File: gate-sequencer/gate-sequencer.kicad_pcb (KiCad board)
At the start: 2 copper layers, 168.4 x 345.6 mm, 172 parts, among them J1 Power, J10 Gate 6, J11 Gate 7, J12 Gate 8, J13 Gate 9, J14 Gate 10, J15 Gate 11, J16 Gate 13, J17 Gate 12, J18 Gate 14, J19 Gate 15, J2 Power, J20 Gate 16, J21 Conn_01x34_Socket, J22 Clock, J23 Gate 1, J24 LED, J25 Gate 2, J26 LED, J27 LED, J28 LED, J29 Gate 3, J3 Power, J30 Gate 4, J31 Gate 5, J32 LED, J33 LED, J34 Gate 6, J35 LED, J36 LED, J37 Gate 7, J38 Gate 8, J39 LED, J4 Clock, J40 Gate 9, J41 LED, J42 Gate 10, J43 LED, J44 Gate 11, J45 LED, J46 LED, J47 Gate 13, J48 Gate 12, J49 Gate 14, J5 Gate 1, J50 LED, J51 Gate 15, J52 LED, J53 LED, J54 Gate 16, J55 Conn_01x34_Pin, J6 Gate 2, J7 Gate 3, J8 Gate 5, J9 Gate 4, SW1 Mode 2, SW10 S3, SW11 S4, SW12 S5, SW13 S6, SW14 S7, SW15 S8, SW16 S9, SW17 S10, SW18 S11, SW19 S12, SW2 Mode, SW20 S13, SW21 S14, SW22 S15, SW23 S16, SW3 Clock Source, SW4 X1, SW5 X2, SW6 X3, SW7 X4, SW8 S1, SW9 S2

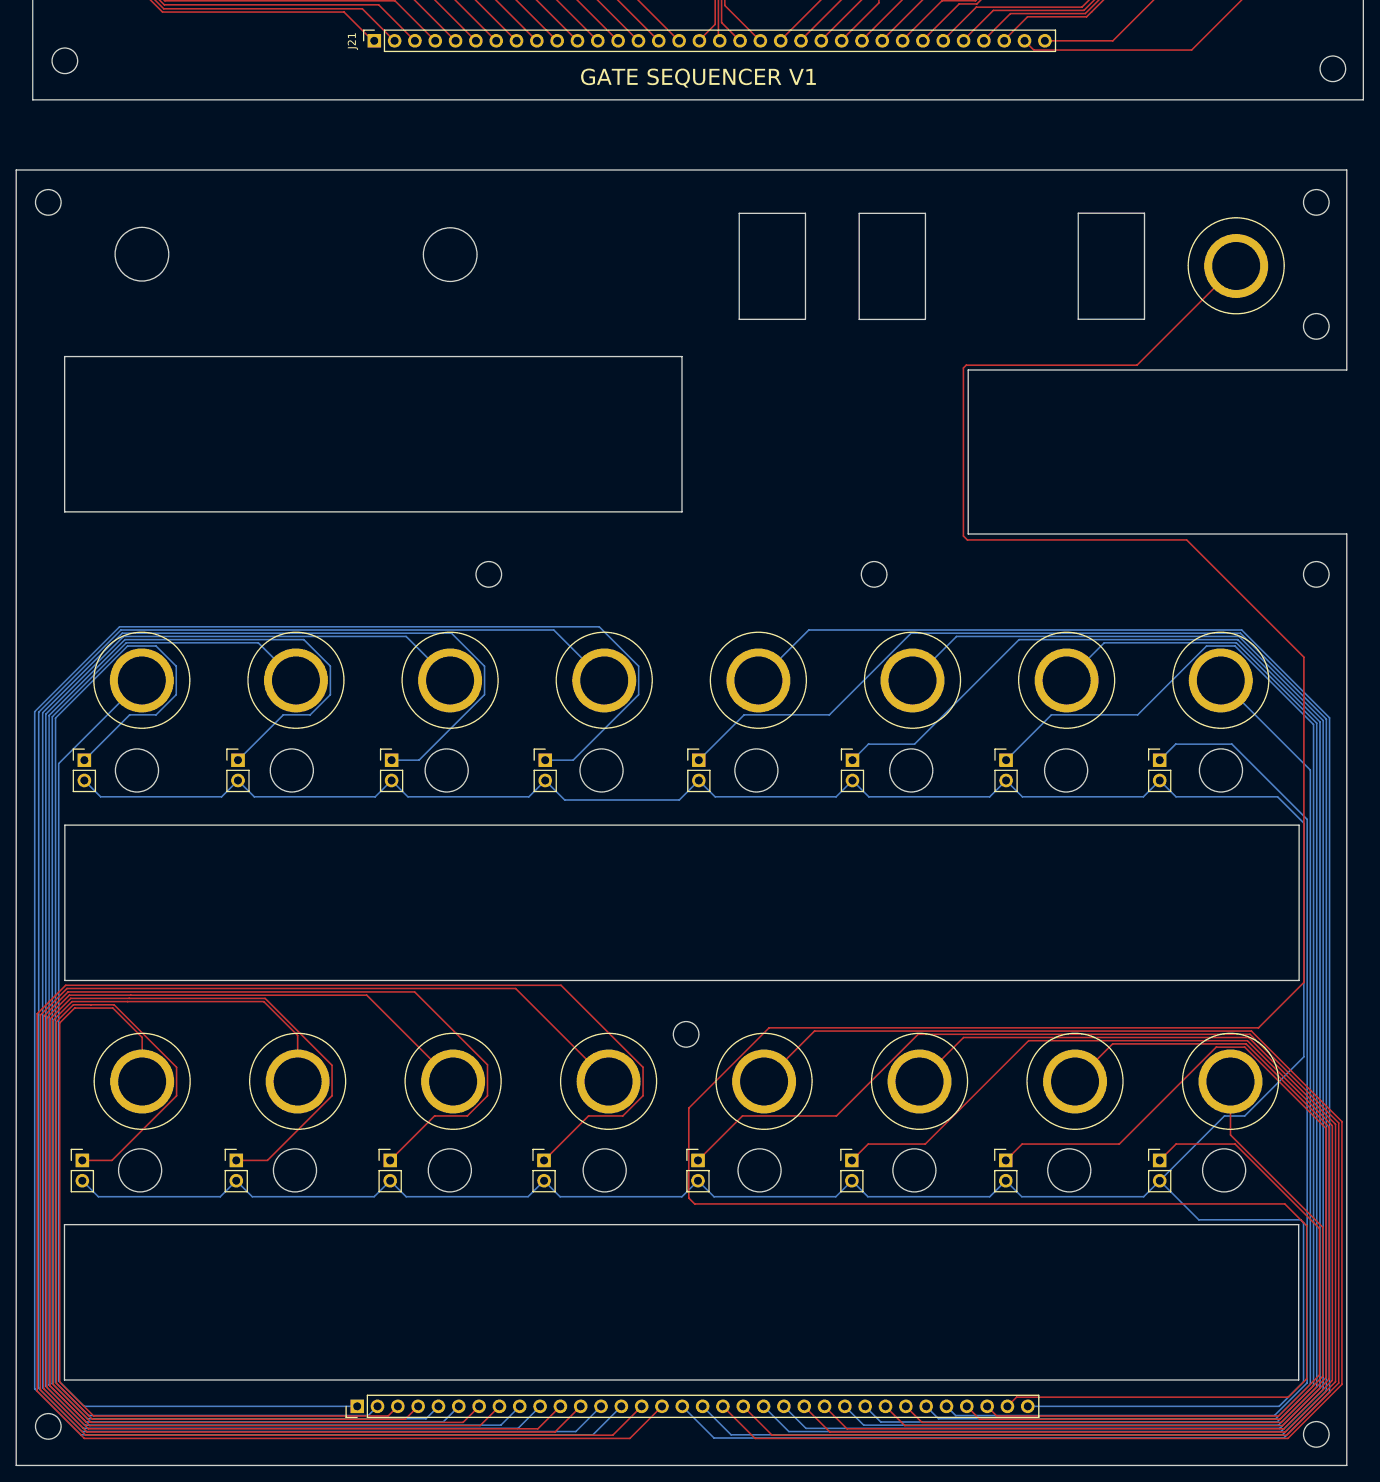
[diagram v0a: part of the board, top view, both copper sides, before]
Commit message: Start firmware for gate sequencer
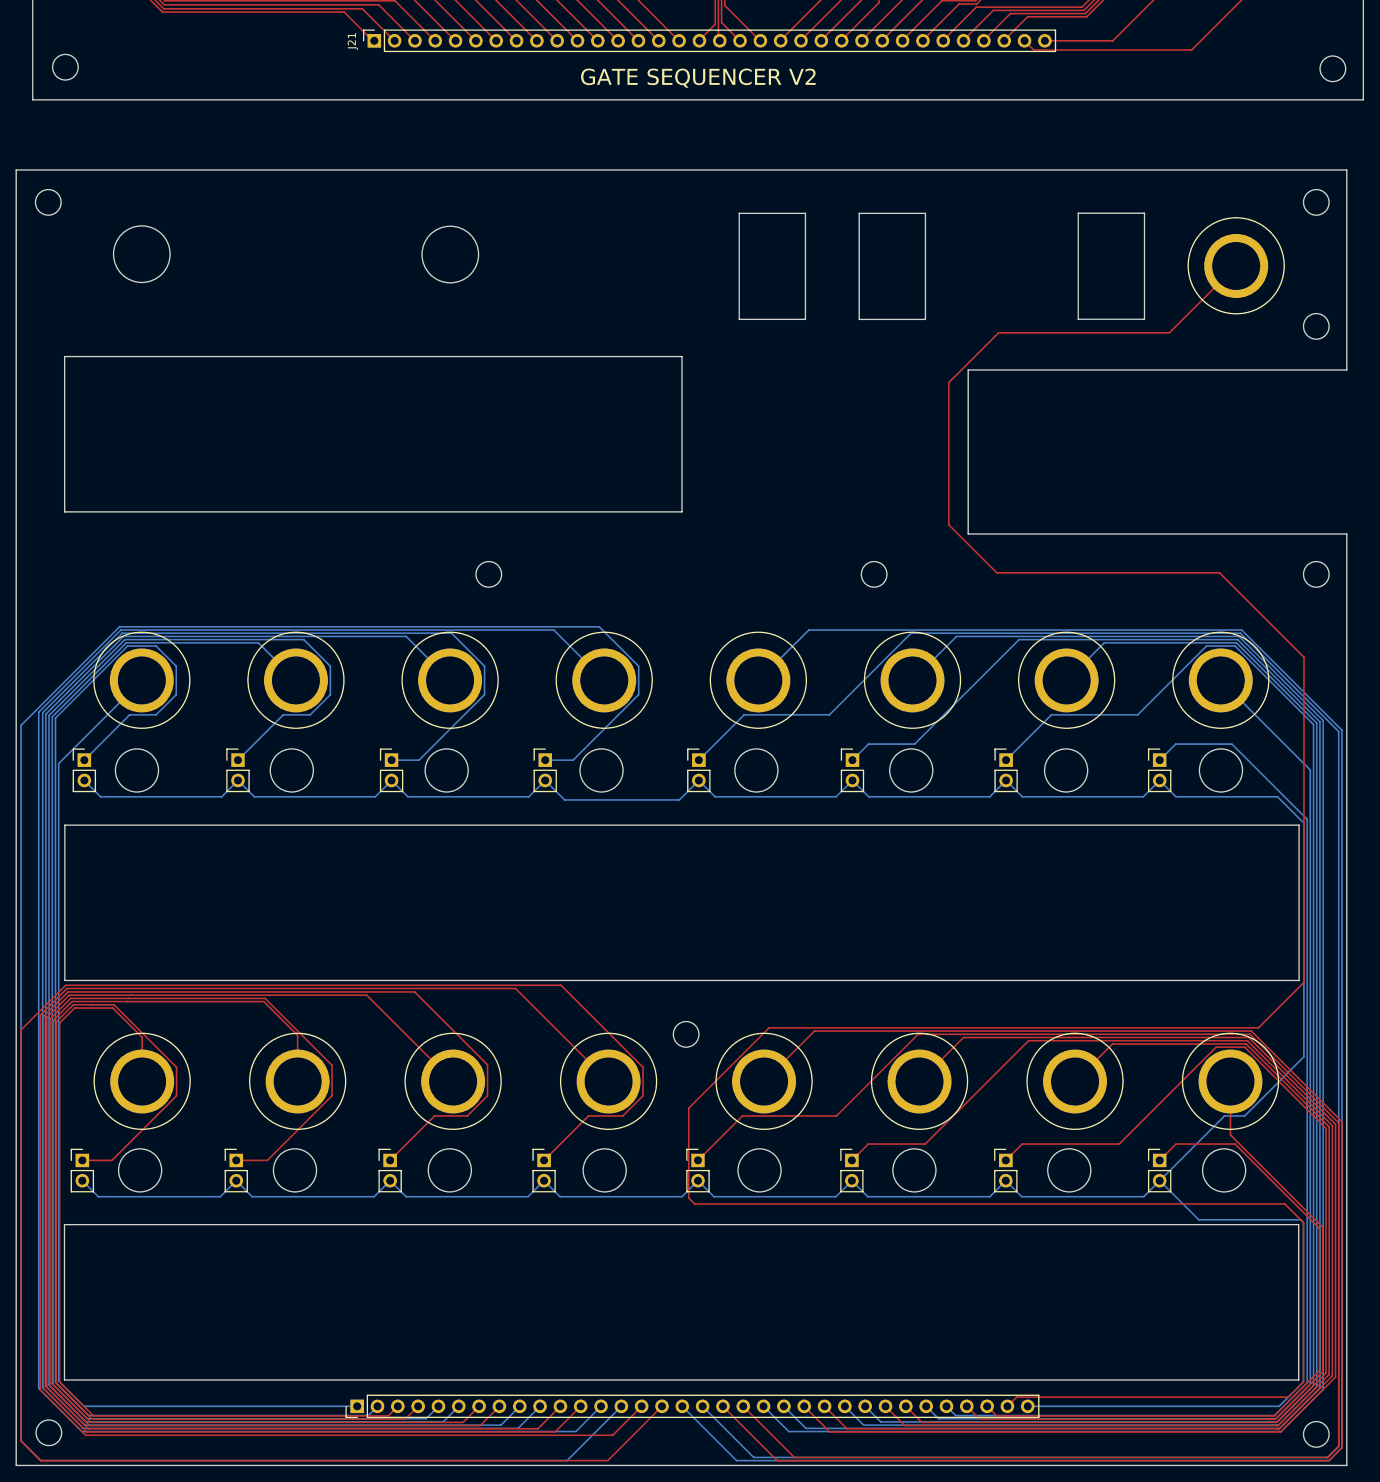
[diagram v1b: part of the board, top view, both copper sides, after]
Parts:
- moved REF** 0.81 mm to (20.5, 347.5)
- moved REF** 0.81 mm to (22.6, 176.8)
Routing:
- net Net-(J28-Pin_1): track 262.4 -> 271.3 mm
- net Net-(J45-Pin_1): track 230.1 -> 238.9 mm
- net Net-(J31-Pin_1): track 247.8 -> 256.4 mm
- net Net-(J32-Pin_1): track 255.1 -> 263.7 mm
- net Net-(J47-Pin_1): track 194.2 -> 201.2 mm
- net Net-(J46-Pin_1): track 202.4 -> 209.3 mm
- net Net-(J22-Pin_1): track 381.2 -> 382.6 mm
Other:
- outline, holes or cut-outs redrawn
- board text added: "GATE SEQUENCER V2"
- board text removed: "GATE SEQUENCER V1"

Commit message: Update some designs
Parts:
- added REF**: MountingHole_3.2mm_M3, MountingHole:MountingHole_3.2mm_M3, F.Cu at (44.7, 280.2)
- added REF**: MountingHole_3.2mm_M3, MountingHole:MountingHole_3.2mm_M3, F.Cu at (160.3, 280.2)
- added REF**: MountingHole_3.2mm_M3, MountingHole:MountingHole_3.2mm_M3, F.Cu at (161.4, 330.2)
- added REF**: MountingHole_3.2mm_M3, MountingHole:MountingHole_3.2mm_M3, F.Cu at (45.5, 91.6)
- added REF**: MountingHole_3.2mm_M3, MountingHole:MountingHole_3.2mm_M3, F.Cu at (161.1, 91.6)
- added REF**: MountingHole_3.2mm_M3, MountingHole:MountingHole_3.2mm_M3, F.Cu at (162.2, 141.6)
- added REF**: MountingHole_3.2mm_M3, MountingHole:MountingHole_3.2mm_M3, F.Cu at (44.9, 330.2)
- added REF**: MountingHole_3.2mm_M3, MountingHole:MountingHole_3.2mm_M3, F.Cu at (45.6, 141.6)
- moved REF** 32.7 mm to (103.1, 330.2)
- moved J23 28.2 mm to (35.1, 281.5)
- moved J24 28.2 mm to (27.9, 291.4)
- moved J25 28.2 mm to (54.4, 281.5)
- moved J26 28.2 mm to (47.1, 291.4)
- moved J27 28.2 mm to (66.3, 291.4)
- moved J28 28.2 mm to (85.5, 291.4)
- moved J29 28.2 mm to (73.6, 281.5)
- moved J30 28.2 mm to (92.9, 281.5)
- moved J31 28.2 mm to (112.2, 281.5)
- moved J32 28.2 mm to (104.7, 291.4)
- moved J33 28.2 mm to (123.9, 291.4)
- moved J34 28.2 mm to (131.4, 281.5)
- moved J35 28.2 mm to (162.3, 291.4)
- moved J36 28.2 mm to (143.1, 291.4)
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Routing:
- net Net-(D20-A): track 112.8 -> 115.6 mm
- net Net-(J12-Pin_1): track 135.8 -> 138.6 mm
- net Net-(J21-Pin_5): track 134.6 -> 137.2 mm
- net Net-(D6-A): track 115.6 -> 118.1 mm
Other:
- board size 168.4 x 345.6 mm -> 167.1 x 363.5 mm

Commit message: Gate sequencer fixes
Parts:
- added D37: 1N4148, Diode_THT:D_DO-35_SOD27_P7.62mm_Horizontal, F.Cu at (36.3, 109.3)
- added D38: 1N4148, Diode_THT:D_DO-35_SOD27_P7.62mm_Horizontal, F.Cu at (113.8, 108.9)
- added D39: 1N4148, Diode_THT:D_DO-35_SOD27_P7.62mm_Horizontal, F.Cu at (36.3, 159.2)
- added D40: 1N4148, Diode_THT:D_DO-35_SOD27_P7.62mm_Horizontal, F.Cu at (113.2, 159.4)
- added D41: 1N4148, Diode_THT:D_DO-35_SOD27_P7.62mm_Horizontal, F.Cu at (55.4, 159.3)
- added D42: 1N4148, Diode_THT:D_DO-35_SOD27_P7.62mm_Horizontal, F.Cu at (132.6, 109.5)
- added D43: 1N4148, Diode_THT:D_DO-35_SOD27_P7.62mm_Horizontal, F.Cu at (55.8, 109.5)
- added D44: 1N4148, Diode_THT:D_DO-35_SOD27_P7.62mm_Horizontal, F.Cu at (132.8, 159.5)
- added D45: 1N4148, Diode_THT:D_DO-35_SOD27_P7.62mm_Horizontal, F.Cu at (75.1, 109.5)
- added D46: 1N4148, Diode_THT:D_DO-35_SOD27_P7.62mm_Horizontal, F.Cu at (152.3, 109.5)
- added D47: 1N4148, Diode_THT:D_DO-35_SOD27_P7.62mm_Horizontal, F.Cu at (74.6, 159.5)
- added D48: 1N4148, Diode_THT:D_DO-35_SOD27_P7.62mm_Horizontal, F.Cu at (152.1, 159.5)
- added D49: 1N4148, Diode_THT:D_DO-35_SOD27_P7.62mm_Horizontal, F.Cu at (94.5, 109.6)
- added D50: 1N4148, Diode_THT:D_DO-35_SOD27_P7.62mm_Horizontal, F.Cu at (171.6, 109.5)
- added D51: 1N4148, Diode_THT:D_DO-35_SOD27_P7.62mm_Horizontal, F.Cu at (94.1, 159.5)
- added D52: 1N4148, Diode_THT:D_DO-35_SOD27_P7.62mm_Horizontal, F.Cu at (171.1, 159.5)
- moved R14 10.7 mm to (118.0, 98.9), turned to -90 degrees
- moved R26 10.6 mm to (41.0, 149.0), turned to -90 degrees
- moved R10 10.4 mm to (40.5, 99.2), turned to -90 degrees
- moved R33 10.3 mm to (176.0, 149.3), turned to -90 degrees
- moved R32 10.2 mm to (157.0, 149.5), turned to -90 degrees
- moved R16 10.2 mm to (156.5, 99.4), turned to -90 degrees
- moved R28 10.2 mm to (79.5, 149.4), turned to -90 degrees
- moved R29 10.2 mm to (99.0, 149.5), turned to -90 degrees
- moved R31 10.2 mm to (137.5, 149.5), turned to -90 degrees
- moved R11 10.1 mm to (59.5, 99.3), turned to -90 degrees
- moved R13 10.1 mm to (98.5, 99.4), turned to -90 degrees
- moved R15 10.1 mm to (137.0, 99.4), turned to -90 degrees
- moved R17 10.1 mm to (175.5, 99.4), turned to -90 degrees
- moved R27 10.1 mm to (60.0, 149.4), turned to -90 degrees
- moved R12 10.1 mm to (79.0, 99.4), turned to -90 degrees
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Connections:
- R10 pad 2: Net-(U1-S0) -> Net-(D37-K)
- R11 pad 2: Net-(U1-S1) -> Net-(D43-K)
- R12 pad 2: Net-(U1-S2) -> Net-(D45-K)
- R13 pad 2: Net-(U1-S3) -> Net-(D49-K)
- R14 pad 2: Net-(U1-S4) -> Net-(D38-K)
- R15 pad 2: Net-(U1-S5) -> Net-(D42-K)
- R16 pad 2: Net-(U1-S6) -> Net-(D46-K)
- R17 pad 2: Net-(U1-S7) -> Net-(D50-K)
- R18 pad 2: Net-(U1-S8) -> Net-(D39-A)
- R19 pad 2: Net-(U1-S9) -> Net-(D41-A)
- R2 pad 2: Net-(U1-S0) -> Net-(D37-A)
- R20 pad 2: Net-(U1-S11) -> Net-(D51-A)
- R21 pad 2: Net-(U1-S10) -> Net-(D47-A)
- R22 pad 2: Net-(U1-S12) -> Net-(D40-A)
- R23 pad 2: Net-(U1-S13) -> Net-(D44-A)
- R24 pad 2: Net-(U1-S14) -> Net-(D48-A)
- R25 pad 2: Net-(U1-S15) -> Net-(D52-A)
- R26 pad 2: Net-(U1-S8) -> Net-(D39-K)
- R27 pad 2: Net-(U1-S9) -> Net-(D41-K)
- R28 pad 2: Net-(U1-S10) -> Net-(D47-K)
- R29 pad 2: Net-(U1-S11) -> Net-(D51-K)
- R3 pad 2: Net-(U1-S1) -> Net-(D43-A)
- R30 pad 2: Net-(U1-S12) -> Net-(D40-K)
- R31 pad 2: Net-(U1-S13) -> Net-(D44-K)
- R32 pad 2: Net-(U1-S14) -> Net-(D48-K)
- R33 pad 2: Net-(U1-S15) -> Net-(D52-K)
- R4 pad 2: Net-(U1-S3) -> Net-(D49-A)
- R5 pad 2: Net-(U1-S2) -> Net-(D45-A)
- R6 pad 2: Net-(U1-S4) -> Net-(D38-A)
- R7 pad 2: Net-(U1-S5) -> Net-(D42-A)
- R8 pad 2: Net-(U1-S6) -> Net-(D46-A)
- R9 pad 2: Net-(U1-S7) -> Net-(D50-A)
- U1 pad 10: Net-(U1-S2) -> Net-(D45-A)
- U1 pad 11: Net-(U1-S0) -> Net-(D37-A)
- U1 pad 13: Net-(U1-S13) -> Net-(D44-A)
- U1 pad 14: Net-(U1-S12) -> Net-(D40-A)
- U1 pad 15: Net-(U1-S15) -> Net-(D52-A)
- U1 pad 16: Net-(U1-S14) -> Net-(D48-A)
- U1 pad 17: Net-(U1-S9) -> Net-(D41-A)
- U1 pad 18: Net-(U1-S8) -> Net-(D39-A)
- U1 pad 19: Net-(U1-S11) -> Net-(D51-A)
- U1 pad 20: Net-(U1-S10) -> Net-(D47-A)
- U1 pad 4: Net-(U1-S7) -> Net-(D50-A)
- U1 pad 5: Net-(U1-S6) -> Net-(D46-A)
- U1 pad 6: Net-(U1-S5) -> Net-(D42-A)
- U1 pad 7: Net-(U1-S4) -> Net-(D38-A)
- U1 pad 8: Net-(U1-S3) -> Net-(D49-A)
- U1 pad 9: Net-(U1-S1) -> Net-(D43-A)
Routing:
- net Net-(U1-S15): track 277.0 -> 0.00 mm
- net Net-(D52-A): track 0.00 -> 277.0 mm
- net Net-(U1-S14): track 258.6 -> 0.00 mm
- net Net-(D48-A): track 0.00 -> 258.5 mm
- net Net-(U1-S13): track 225.1 -> 0.00 mm
- net Net-(D44-A): track 0.00 -> 225.1 mm
- net Net-(U1-S12): track 201.7 -> 0.00 mm
- net Net-(D40-A): track 0.00 -> 201.7 mm
- net Net-(U1-S7): track 180.5 -> 0.00 mm
- net Net-(D50-A): track 0.00 -> 180.5 mm
- net Net-(U1-S11): track 168.1 -> 0.00 mm
- net Net-(D51-A): track 0.00 -> 168.1 mm
- net Net-(U1-S6): track 162.4 -> 0.00 mm
- net Net-(D46-A): track 0.00 -> 162.4 mm
- net Net-(U1-S5): track 144.3 -> 0.00 mm
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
